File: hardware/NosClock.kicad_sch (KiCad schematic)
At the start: 15 parts, among them J101 AC, J102 USB_C_Receptacle_USB2.0_16P, U103 DS18B20, U104 ESP32-C3-WROOM-02

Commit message: 2/static version
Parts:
- removed J101: AC, NosLib:TerminalBlock_Phoenix_MKDS-1,5-2-5.08_1x02_P5.08mm_Horizontal, symbol Connector:Screw_Terminal_01x02
- removed R101: 10K, Resistor_SMD:R_0603_1608Metric, symbol Device:R
- removed TP_101: BOOT, NosLib:TestPoint_Pad_1.0x1.0mm, symbol Connector:TestPoint
- added H101, H102, H103, H104: MountingHole, MountingHole:MountingHole_3.2mm_M3_Pad_Via, symbol Mechanical:MountingHole_Pad
- added J102: 12V IN, Connector_JST:JST_XH_B2B-XH-A_1x02_P2.50mm_Vertical, symbol Connector_Generic:Conn_01x02
- added NT102, NT103, NT104: NetTie_2, NetTie:NetTie-2_SMD_Pad0.5mm, symbol Device:NetTie_2
- added R102, R103: 4.7K, Resistor_SMD:R_0603_1608Metric_Pad0.98x0.95mm_HandSolder, symbol Device:R
- added TP_102: SDA, NosLib:TestPoint_Pad_1.0x1.0mm, symbol Connector:TestPoint
- added TP_104: SCL, NosLib:TestPoint_Pad_1.0x1.0mm, symbol Connector:TestPoint
- renumbered J102 to J101, NT102 to NT105, R102 to R101, R103 to R104, R104 to R105, R105 to R106, TP_102 to TP_101, U104 to U101, U103 to U102
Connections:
- net 3V3 is gone; now on net +3V3: R101.1
- net 5V is gone; now on net +5V: NT101.2
- net +170V: now also NT102.1
- net +3V3: now also NT103.1, R102.1, R103.1
- net +5V: now also NT104.1
- net DALLAS: now also U101.16 (GPIO2/ADC1_CH2); no longer U101.7 (GPIO8)
- net GND: now also H101.1, H102.1, H103.1, H104.1
- net UC3843/PWR_GND: now also J102.1 (Pin_1)
- net INPUT: now reaches U101.11 (GPIO20/U0RXD)
- net SK6812MINI_DATA: now reaches U101.12 (GPIO21/U0TXD)
- net MUX2: now reaches U101.17 (GPIO1/ADC1_CH1/XTAL_32K_N)
- net MUX1: now reaches U101.18 (GPIO0/ADC1_CH0/XTAL_32K_P)
- net BOOT renamed SCL
- net SCL: now also R103.2, TP_102.1
- net LED renamed INPUT2
- net ~{PWM_DIGITS} renamed MUX3
- net ~{PWM_DOTS} renamed COLONS
- new net MP2307/+12V: J102.2 (Pin_2)
- new net MP2307/+3V3: NT103.2
- new net MP2307/+5V: NT104.2
- new net SDA: R102.2, TP_104.1, U101.7 (GPIO8)
- new net UC3843/+170V: NT102.2
- no-connect marks 6 -> 2
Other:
- removed sheet LDO
- sheet Lamps ports: added +170V, +3V3, +5V, COLONS, CS, LAMP1, LAMP2, LAMP3, SCK, SER, SK6812MINI_DATA; removed none
- sheet MP2307 ports: added +3V3; removed none
- sheet UC3843 ports: added +12V, +170V; removed 12V, 170V
- moved on the sheet: C101, NT105, R101, TP_101, TP_103, U101

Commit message: Battery
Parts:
- removed TP_103: GND, NosLib:TestPoint_Pad_1.0x1.0mm, symbol Connector:TestPoint
- added BT101: Battery_Cell, NosLib:BAT_CH291-1220LF, symbol Device:Battery_Cell
- added C102: 100nF, Capacitor_SMD:C_0603_1608Metric, symbol Device:C
- added J102: Conn_01x04, Connector_Molex:Molex_PicoBlade_53047-0410_1x04_P1.25mm_Vertical, symbol Connector_Generic:Conn_01x04
- added TP_102: GND, NosLib:TestPoint_Pad_1.0x1.0mm, symbol Connector:TestPoint
- added TP_105: +170V, NosLib:TestPoint_Pad_1.0x1.0mm, symbol Connector:TestPoint
- added TP_106: +5V, NosLib:TestPoint_Pad_1.0x1.0mm, symbol Connector:TestPoint
- added TP_107: +3V3, NosLib:TestPoint_Pad_1.0x1.0mm, symbol Connector:TestPoint
- added TP_108: +12V, NosLib:TestPoint_Pad_1.0x1.0mm, symbol Connector:TestPoint
- added U103: DS3231MZ, Package_SO:SOIC-8_3.9x4.9mm_P1.27mm, symbol Timer_RTC:DS3231MZ
- renumbered J102 to J103, TP_102 to TP_103
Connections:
- net +170V: now also TP_105.1
- net +3V3: now also C102.1, J102.2 (Pin_2), TP_107.1, U103.2 (VCC)
- net +5V: now also TP_106.1
- net GND: now also BT101.2 (-), C102.2, J102.1 (Pin_1), TP_102.1, U103.5 (GND)
- net SCL: now also J102.3 (Pin_3), U103.8 (SCL)
- net SDA: now also J102.4 (Pin_4), U103.7 (SDA)
- net MP2307/+12V renamed +12V
- net +12V: now also TP_108.1
- new net: BT101.1 (+), U103.6 (VBAT)
- no-connect marks 2 -> 5
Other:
- note added: "Inputs / outputs"
- note added: "LAMPS"
- moved on the sheet: TP_103, TP_104

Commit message: Finalize schematics
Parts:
- removed NT102: NetTie_2, NetTie:NetTie-2_SMD_Pad0.5mm, symbol Device:NetTie_2
- added C101: 100nF, Capacitor_SMD:C_0603_1608Metric, symbol Device:C
- added J103: Conn_01x02, Connector_JST:JST_PH_B2B-PH-K_1x02_P2.00mm_Vertical, symbol Connector_Generic:Conn_01x02
- added TP_101: DBG, NosLib:TestPoint_Pad_1.0x1.0mm, symbol Connector:TestPoint
- added TP_102, TP_111: GND, NosLib:TestPoint_Pad_1.0x1.0mm, symbol Connector:TestPoint
- TP_107: renamed from TP_105; value +170V -> 170V
- TP_108: renamed from TP_106; value +5V -> 5V
- TP_109: renamed from TP_107; value +3V3 -> 3V3
- TP_110: renamed from TP_108; value +12V -> 12V
- renumbered C101 to C102, C102 to C103, J102 to J101, J101 to J102, J103 to J104, NT103 to NT102, NT104 to NT103, NT105 to NT104, TP_101 to TP_103, TP_102 to TP_104, TP_103 to TP_105, TP_104 to TP_106
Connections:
- net +3V3: now also C101.1
- net GND: now also C101.2, J103.2 (Pin_2), TP_102.1, TP_111.1
- net INPUT: now also J103.1 (Pin_1)
- net INPUT2 renamed DBG
- net DBG: now also TP_101.1
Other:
- moved on the sheet: J101, TP_107, TP_108, TP_109, TP_110

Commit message: Fixes
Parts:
- R102, R103: footprint Resistor_SMD:R_0603_1608Metric_Pad0.98x0.95mm_HandSolder -> Resistor_SMD:R_0603_1608Metric
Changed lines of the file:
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@@
 			)
 		)
-		(property "Footprint" "Resistor_SMD:R_0603_1608Metric_Pad0.98x0.95mm_HandSolder"
+		(property "Footprint" "Resistor_SMD:R_0603_1608Metric"
 			(at 59.69 34.798 90)
 			(effects
@@
 			)
 		)
-		(property "Footprint" "Resistor_SMD:R_0603_1608Metric_Pad0.98x0.95mm_HandSolder"
+		(property "Footprint" "Resistor_SMD:R_0603_1608Metric"
 			(at 59.69 37.338 90)
 			(effects

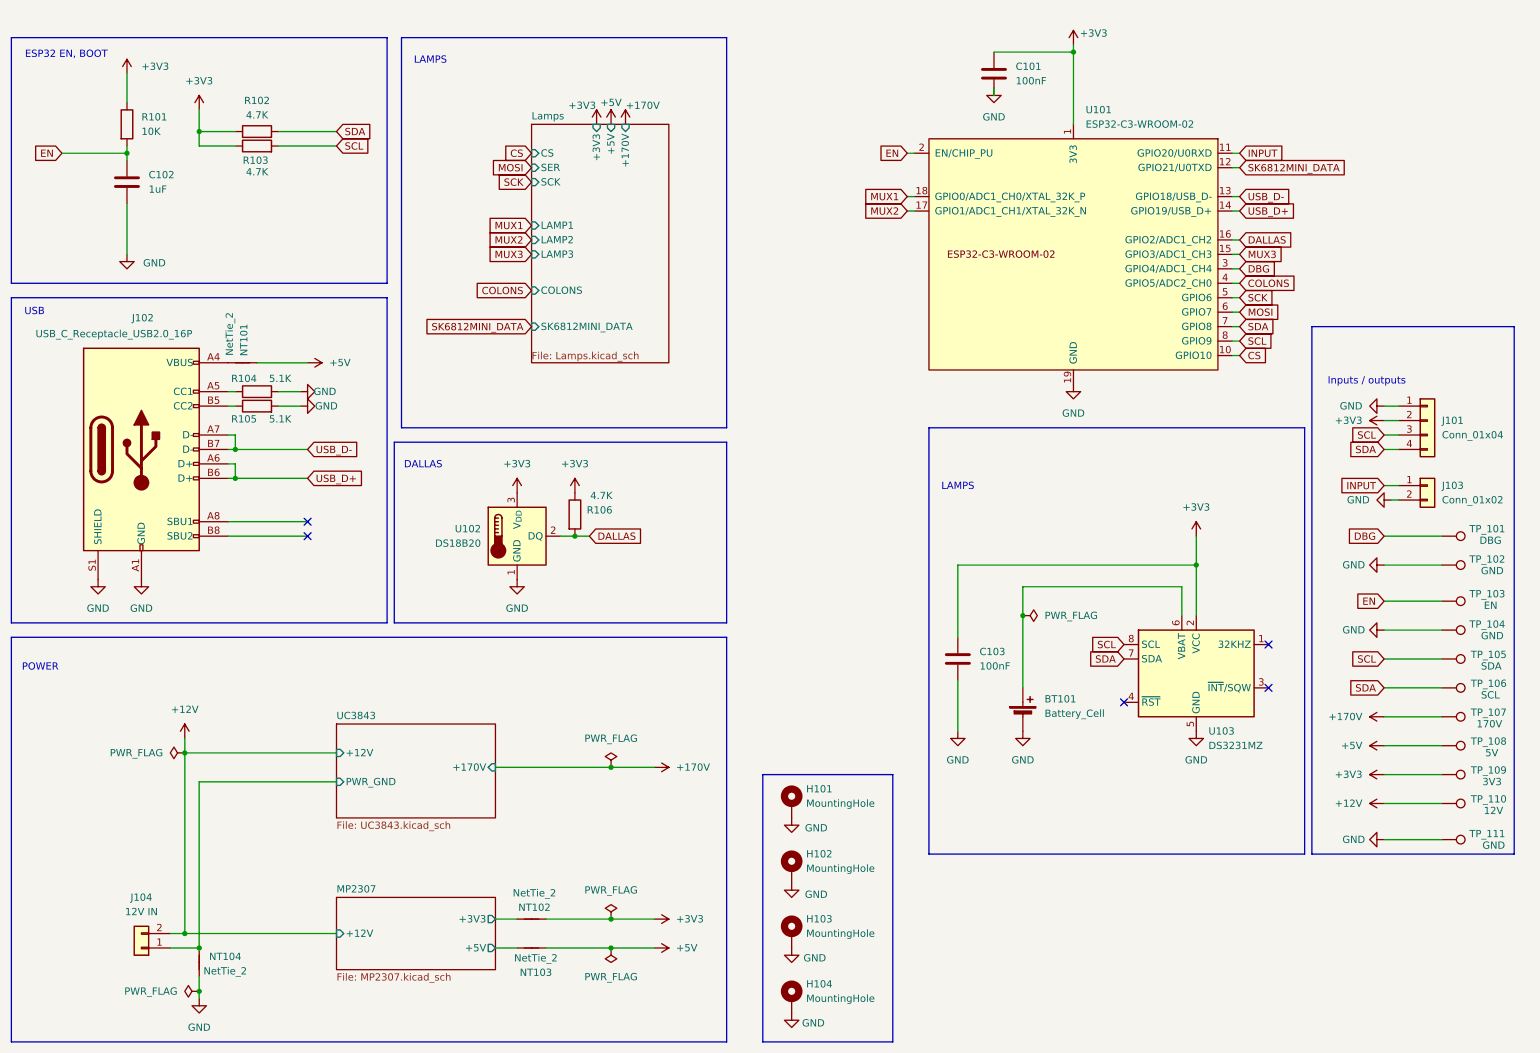
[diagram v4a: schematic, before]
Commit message: Lamps tracing
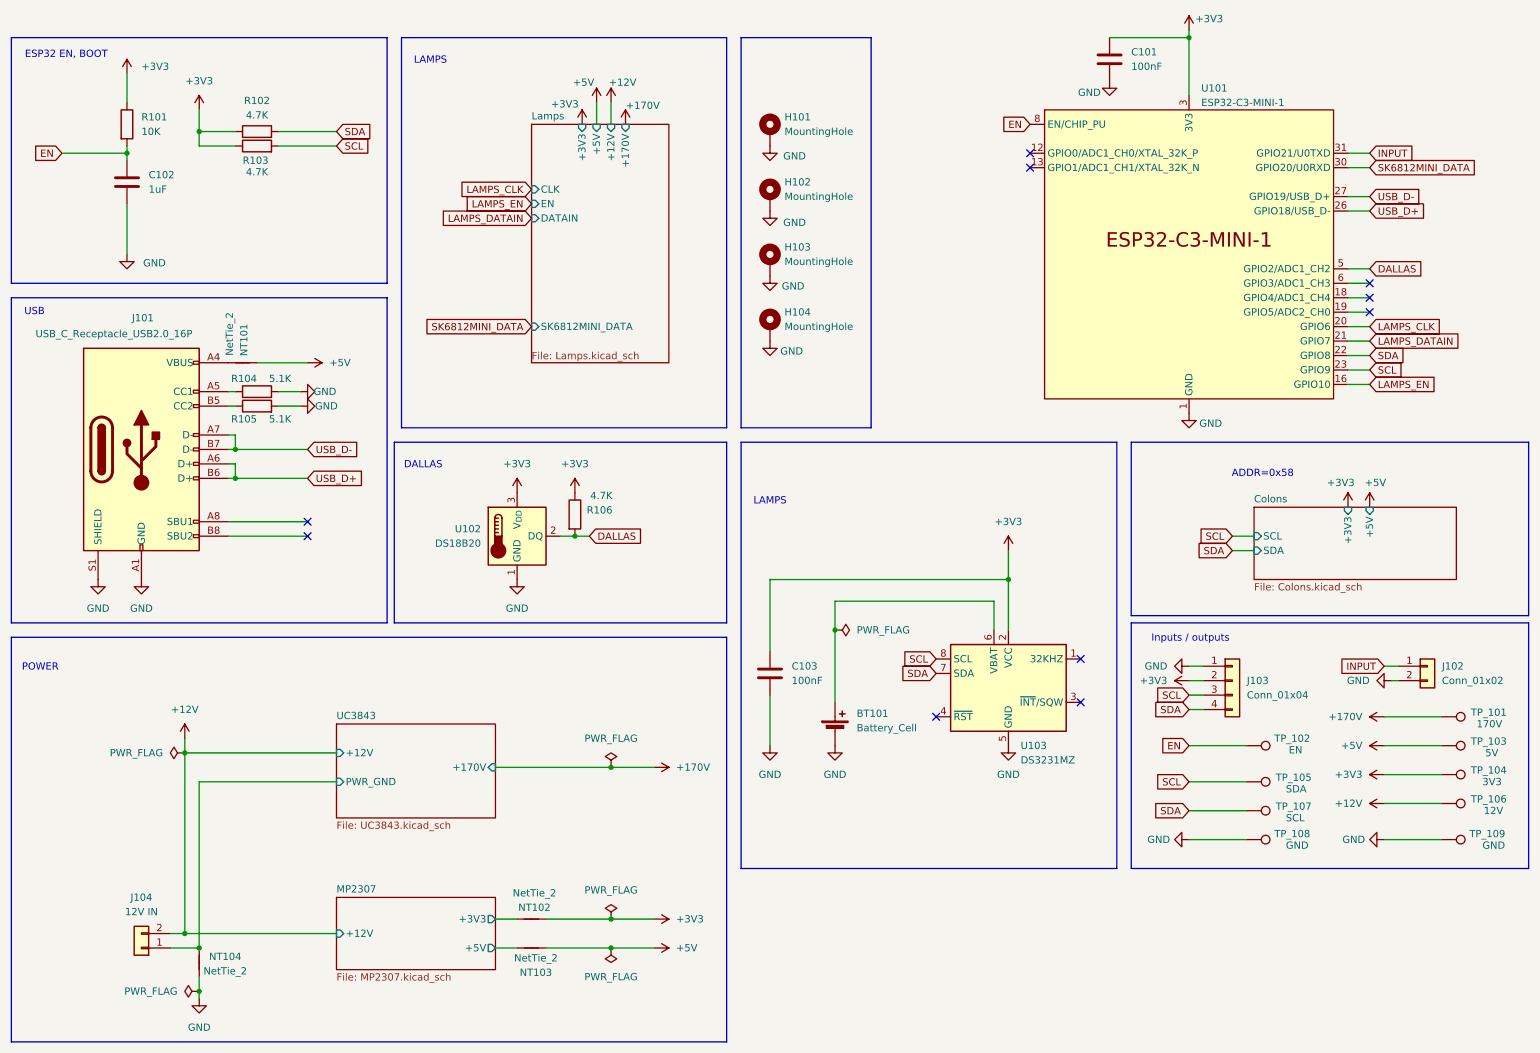
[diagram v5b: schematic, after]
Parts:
- removed TP_101: DBG, NosLib:TestPoint_Pad_1.0x1.0mm, symbol Connector:TestPoint
- removed TP_102: GND, NosLib:TestPoint_Pad_1.0x1.0mm, symbol Connector:TestPoint
- removed U101: ESP32-C3-WROOM-02, PCM_Espressif:ESP32-C3-WROOM-02, symbol PCM_Espressif:ESP32-C3-WROOM-02
- added U101: ESP32-C3-MINI-1, PCM_Espressif:ESP32-C3-MINI-1, symbol PCM_Espressif:ESP32-C3-MINI-1
- renumbered J102 to J101, J103 to J102, J101 to J103, TP_107 to TP_101, TP_103 to TP_102, TP_108 to TP_103, TP_109 to TP_104, TP_110 to TP_106, TP_106 to TP_107, TP_104 to TP_108, TP_111 to TP_109
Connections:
- net +3V3: now also U101.3 (3V3)
- net DALLAS: now also U101.5 (GPIO2/ADC1_CH2)
- net EN: now also U101.8 (EN/CHIP_PU)
- net GND: now also U101.1 (GND), U101.11 (GND), U101.14 (GND), U101.2 (GND), U101.36 (GND), U101.37 (GND), U101.38 (GND), U101.39 (GND), U101.40 (GND), U101.41 (GND), U101.42 (GND), U101.43 (GND), U101.44 (GND), U101.45 (GND), U101.46 (GND), U101.47 (GND), U101.48 (GND), U101.49 (GND), U101.50 (GND), U101.51 (GND), U101.52 (GND), U101.53 (GND)
- net INPUT: now also U101.31 (GPIO21/U0TXD)
- net SCL: now also U101.23 (GPIO9)
- net SDA: now also U101.22 (GPIO8)
- net SK6812MINI_DATA: now also U101.30 (GPIO20/U0RXD)
- net USB_D+: now also U101.26 (GPIO18/USB_D-)
- net USB_D-: now also U101.27 (GPIO19/USB_D+)
- new net LAMPS_CLK: U101.20 (GPIO6)
- new net LAMPS_DATAIN: U101.21 (GPIO7)
- new net LAMPS_EN: U101.16 (GPIO10)
- no-connect marks 5 -> 10
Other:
- added sheet Colons (Colons.kicad_sch)
- sheet Lamps ports: added +12V, CLK, DATAIN, EN; removed COLONS, CS, LAMP1, LAMP2, LAMP3, SCK, SER
- note added: "ADDR=0x58"
- moved on the sheet: BT101, C103, H101, H102, H103, H104, J102, J103, TP_102, TP_105, TP_107, TP_108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

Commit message: almost ready but need to redesign
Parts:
- removed R106: 4.7K, Resistor_SMD:R_0603_1608Metric, symbol Device:R
- removed U102: DS18B20, Package_TO_SOT_THT:TO-92_Inline, symbol Sensor_Temperature:DS18B20
- added NT106: NetTie_2, NetTie:NetTie-2_SMD_Pad0.5mm, symbol Device:NetTie_2
- added TP_110: GND, NosLib:TestPoint_Pad_1.0x1.0mm, symbol Connector:TestPoint
- TP_105: value SDA -> SDA/BOOT
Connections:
- net +12V: now also NT106.1; no longer J104.2 (Pin_2)
- net GND: now also TP_110.1
- net DALLAS: no longer names the net of U101.5 (GPIO2/ADC1_CH2)
- new net MP2307/+12V: J104.2 (Pin_2), NT106.2
- no-connect marks 10 -> 12
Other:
- note added: "TIME"
- note removed: "DALLAS"
- moved on the sheet: C101, TP_108, TP_109, U101

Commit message: connect all
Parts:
- removed NT102, NT103: NetTie_2, NetTie:NetTie-2_SMD_Pad0.5mm, symbol Device:NetTie_2
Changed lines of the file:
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@@
 	(wire
 		(pts
-			(xy 121.92 171.45) (xy 110.49 171.45)
-		)
-		(stroke
-			(width 0)
-			(type default)
-		)
-	)
-	(wire
-		(pts
 			(xy 226.06 127) (xy 223.52 127)
 		)
@@
 	(wire
 		(pts
-			(xy 121.92 176.53) (xy 110.49 176.53)
-		)
-		(stroke
-			(width 0)
-			(type default)
-		)
-	)
-	(wire
-		(pts
 			(xy 255.27 71.12) (xy 251.46 71.12)
 		)
@@
 	(wire
 		(pts
-			(xy 101.6 176.53) (xy 105.41 176.53)
+			(xy 101.6 176.53) (xy 121.92 176.53)
 		)
 		(stroke
@@
 	(wire
 		(pts
-			(xy 101.6 171.45) (xy 105.41 171.45)
+			(xy 101.6 171.45) (xy 121.92 171.45)
 		)
 		(stroke
@@
 					(unit 1)
 				)
-				(path "/5a46aee9-b968-477e-a4a1-4edba06163a3/cbfce168-24b0-4ff9-a45f-71f9f499ca5c/be8b82a5-add1-4f70-b173-db026f30f284"
-					(reference "BT101")
-					(unit 1)
-				)
 			)
 		)
@@
 	)
 	(symbol
-		(lib_id "Device:NetTie_2")
-		(at 107.95 171.45 180)
-		(unit 1)
-		(body_style 1)
-		(exclude_from_sim no)
-		(in_bom no)
-		(on_board yes)
-		(in_pos_files yes)
-		(dnp no)
-		(property "Reference" "NT102"
-			(at 108.458 169.418 0)
-			(show_name no)
-			(do_not_autoplace no)
-			(effects
-				(font
-					(size 1.27 1.27)
-				)
-			)
-		)
-		(property "Value" "NetTie_2"
-			(at 108.458 166.878 0)
-			(show_name no)
-			(do_not_autoplace no)
-			(effects
-				(font
-					(size 1.27 1.27)
-				)
-			)
-		)
-		(property "Footprint" "NetTie:NetTie-2_SMD_Pad0.5mm"
-			(at 107.95 171.45 0)
-			(hide yes)
-			(show_name no)
-			(do_not_autoplace no)
-			(effects
-				(font
-					(size 1.27 1.27)
-				)
-			)
-		)
-		(property "Datasheet" ""
-			(at 107.95 171.45 0)
-			(hide yes)
-			(show_name no)
-			(do_not_autoplace no)
-			(effects
-				(font
-					(size 1.27 1.27)
-				)
-			)
-		)
-		(property "Description" "Net tie, 2 pins"
-			(at 107.95 171.45 0)
-			(hide yes)
-			(show_name no)
-			(do_not_autoplace no)
-			(effects
-				(font
-					(size 1.27 1.27)
-				)
-			)
-		)
-		(pin "2"
-		)
-		(pin "1"
-		)
-		(instances
-			(project "NosClock"
-				(path "/5a46aee9-b968-477e-a4a1-4edba06163a3"
-					(reference "NT102")
-					(unit 1)
-				)
-			)
-		)
-	)
-	(symbol
 		(lib_id "Connector:TestPoint")
 		(at 267.97 146.05 270)
@@
 	)
 	(symbol
-		(lib_id "Device:NetTie_2")
-		(at 107.95 176.53 180)
-		(unit 1)
-		(body_style 1)
-		(exclude_from_sim no)
-		(in_bom no)
-		(on_board yes)
-		(in_pos_files yes)
-		(dnp no)
-		(property "Reference" "NT103"
-			(at 108.712 180.848 0)
-			(show_name no)
-			(do_not_autoplace no)
-			(effects
-				(font
-					(size 1.27 1.27)
-				)
-			)
-		)
-		(property "Value" "NetTie_2"
-			(at 108.712 178.308 0)
-			(show_name no)
-			(do_not_autoplace no)
-			(effects
-				(font
-					(size 1.27 1.27)
-				)
-			)
-		)
-		(property "Footprint" "NetTie:NetTie-2_SMD_Pad0.5mm"
-			(at 107.95 176.53 0)
-			(hide yes)
-			(show_name no)
-			(do_not_autoplace no)
-			(effects
-				(font
-					(size 1.27 1.27)
-				)
-			)
-		)
-		(property "Datasheet" ""
-			(at 107.95 176.53 0)
-			(hide yes)
-			(show_name no)
-			(do_not_autoplace no)
-			(effects
-				(font
-					(size 1.27 1.27)
-				)
-			)
-		)
-		(property "Description" "Net tie, 2 pins"
-			(at 107.95 176.53 0)
-			(hide yes)
-			(show_name no)
-			(do_not_autoplace no)
-			(effects
-				(font
-					(size 1.27 1.27)
-				)
-			)
-		)
-		(pin "2"
-		)
-		(pin "1"
-		)
-		(instances
-			(project "NosClock"
-				(path "/5a46aee9-b968-477e-a4a1-4edba06163a3"
-					(reference "NT103")
-					(unit 1)
-				)
-			)
-		)
-	)
-	(symbol
 		(lib_id "power:+3.3V")
 		(at 129.54 171.45 270)
@@
 		(in_pos_files yes)
 		(dnp no)
-		(fields_autoplaced yes)
 		(property "Reference" "#PWR0134"
 			(at 261.62 140.97 0)
